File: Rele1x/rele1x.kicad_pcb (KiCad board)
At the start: 2 copper layers, 8 parts, among them J1 TB_1X3, K1 RELAY_C, Q1 2N3904

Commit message: Avances Poncho Rele1x.
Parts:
- added MP?: Plantilla_EDU-CIAA, footprint:Plantilla_EDU-CIAA, F.Cu at (200.0, 92.0)
- moved R1 50.9 mm to (155.0, 96.0), turned to 180 degrees
- moved D1 50.5 mm to (155.0, 104.0), turned to 180 degrees
- moved Q1 48.9 mm to (159.0, 95.0), turned to 270 degrees
- moved R2 41.4 mm to (155.0, 100.0), turned to 180 degrees
- moved LED1 30.4 mm to (159.0, 101.0), turned to 270 degrees
- moved J1 17.5 mm to (150.0, 132.0)
- moved K1 17.5 mm to (150.0, 107.0)
- moved XA1 11.2 mm to (129.0, 92.0)
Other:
- board outline added: 44 x 57 mm

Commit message: Mejoras al ejercicio Rele1x.
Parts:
- removed MP?: Plantilla_EDU-CIAA, footprint:Plantilla_EDU-CIAA
- added G***: LOGO, footprint:Logo_Poncho, F.Cu at (161.0, 127.0)
- added G101: Logo_OSHWA, footprint:Logo_OSHWA, F.Cu at (140.5, 92.0)
- moved Q1 0.50 mm to (159.0, 94.5)
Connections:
- K1 pad 1: Net-(J1-Pad1) -> Net-(J1-Pad2)
- K1 pad 3: Net-(J1-Pad2) -> Net-(J1-Pad1)
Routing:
- net +5VP: track 0.00 -> 54.0 mm
- net Net-(R1-Pad2): track 0.00 -> 43.8 mm
- net Net-(J1-Pad2): track 0.00 -> 25.0 mm
- net Net-(D1-Pad2): track 0.00 -> 24.8 mm
- net Net-(J1-Pad1): track 0.00 -> 11.3 mm
- net Net-(J1-Pad3): track 0.00 -> 11.2 mm
- net Net-(LED1-Pad1): track 0.00 -> 4.41 mm
- net Net-(Q1-Pad2): track 0.00 -> 4.10 mm
- added copper zone on B.Cu, net GNDD
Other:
- net class Default: clearance 0.2 -> 0.5
- rule trace_clearance: 0.2 -> 0.5
- board text added: "Capas: 1 Grilla Posicionamiento: 1 mm Grilla Ruteo: 0,5 mm y 0,25 mm Min ancho pista: 0,8 mm Min ancho pista Q1: 0,6 mm Margen: 0,8 mm Diam Vía/agujero: 1,3/0,7 mm"
- board text added: "NA C NC"
- board text added: "PONCHO RELE1x"

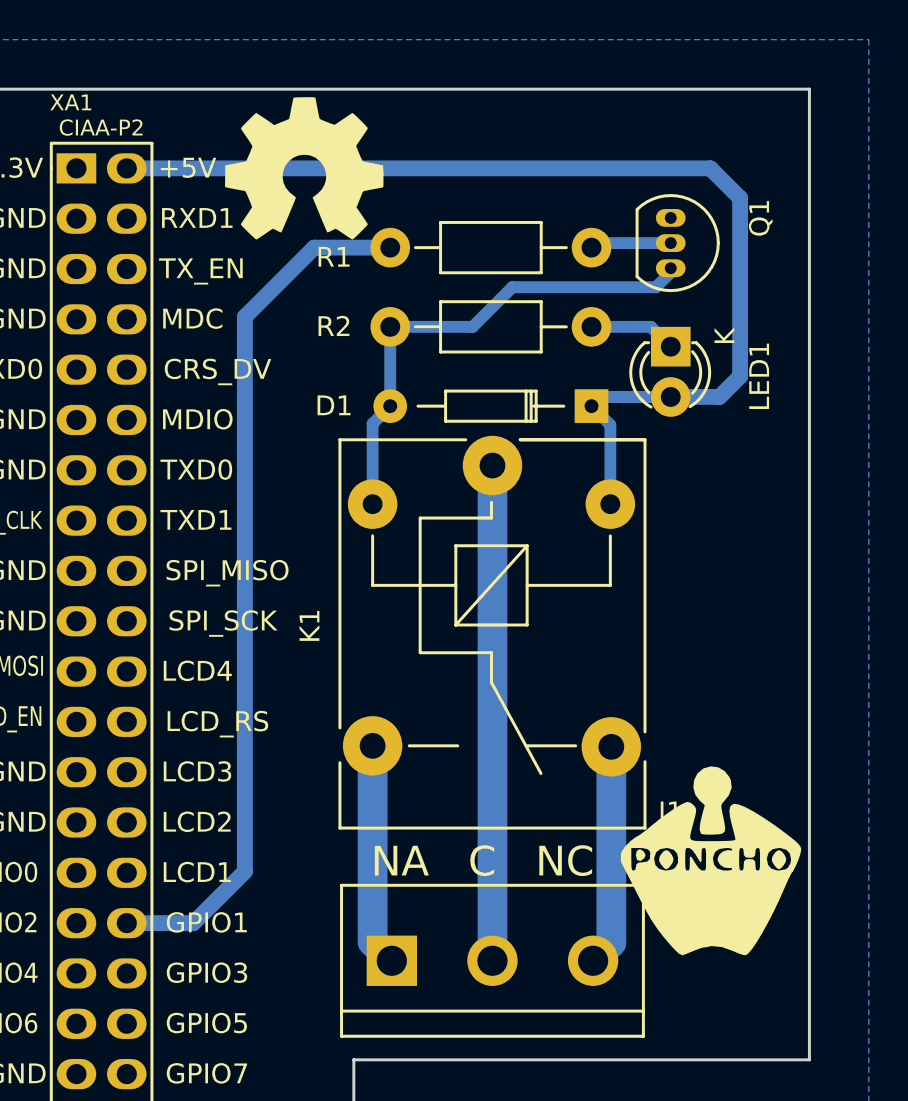
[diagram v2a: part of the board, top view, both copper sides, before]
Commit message: Detalles en el PCB serigrafía, etc.
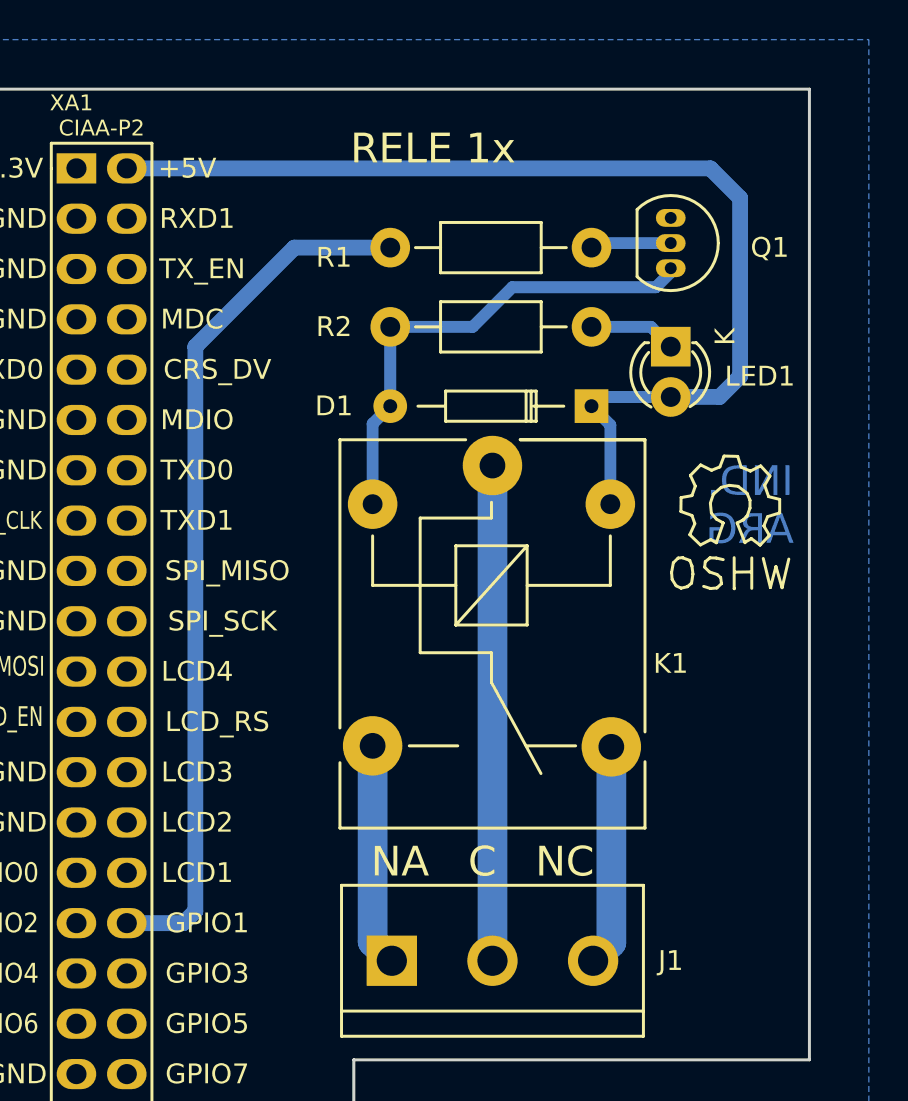
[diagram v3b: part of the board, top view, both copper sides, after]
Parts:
- removed G***: LOGO, footprint:Logo_Poncho
- removed G101: Logo_OSHWA, footprint:Logo_OSHWA
- added REF**: Symbol_OSHW-Logo_SilkScreen, Symbols:Symbol_OSHW-Logo_SilkScreen, F.Cu at (162.0, 109.0)
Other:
- board text added: "Capas: 1 Grilla Posicionamiento: 1 mm Grilla Ruteo: 0,5 mm y 0,25 mm Min ancho pista: 0,8 mm Min ancho pista Q1: 0,6 mm Margen: 0,5 mm Diam Vía/agujero: 1,3/0,7 mm"
- board text added: "IND. ARG"
- board text added: "RELE 1x"
- board text removed: "Capas: 1 Grilla Posicionamiento: 1 mm Grilla Ruteo: 0,5 mm y 0,25 mm Min ancho pista: 0,8 mm Min ancho pista Q1: 0,6 mm Margen: 0,8 mm Diam Vía/agujero: 1,3/0,7 mm"

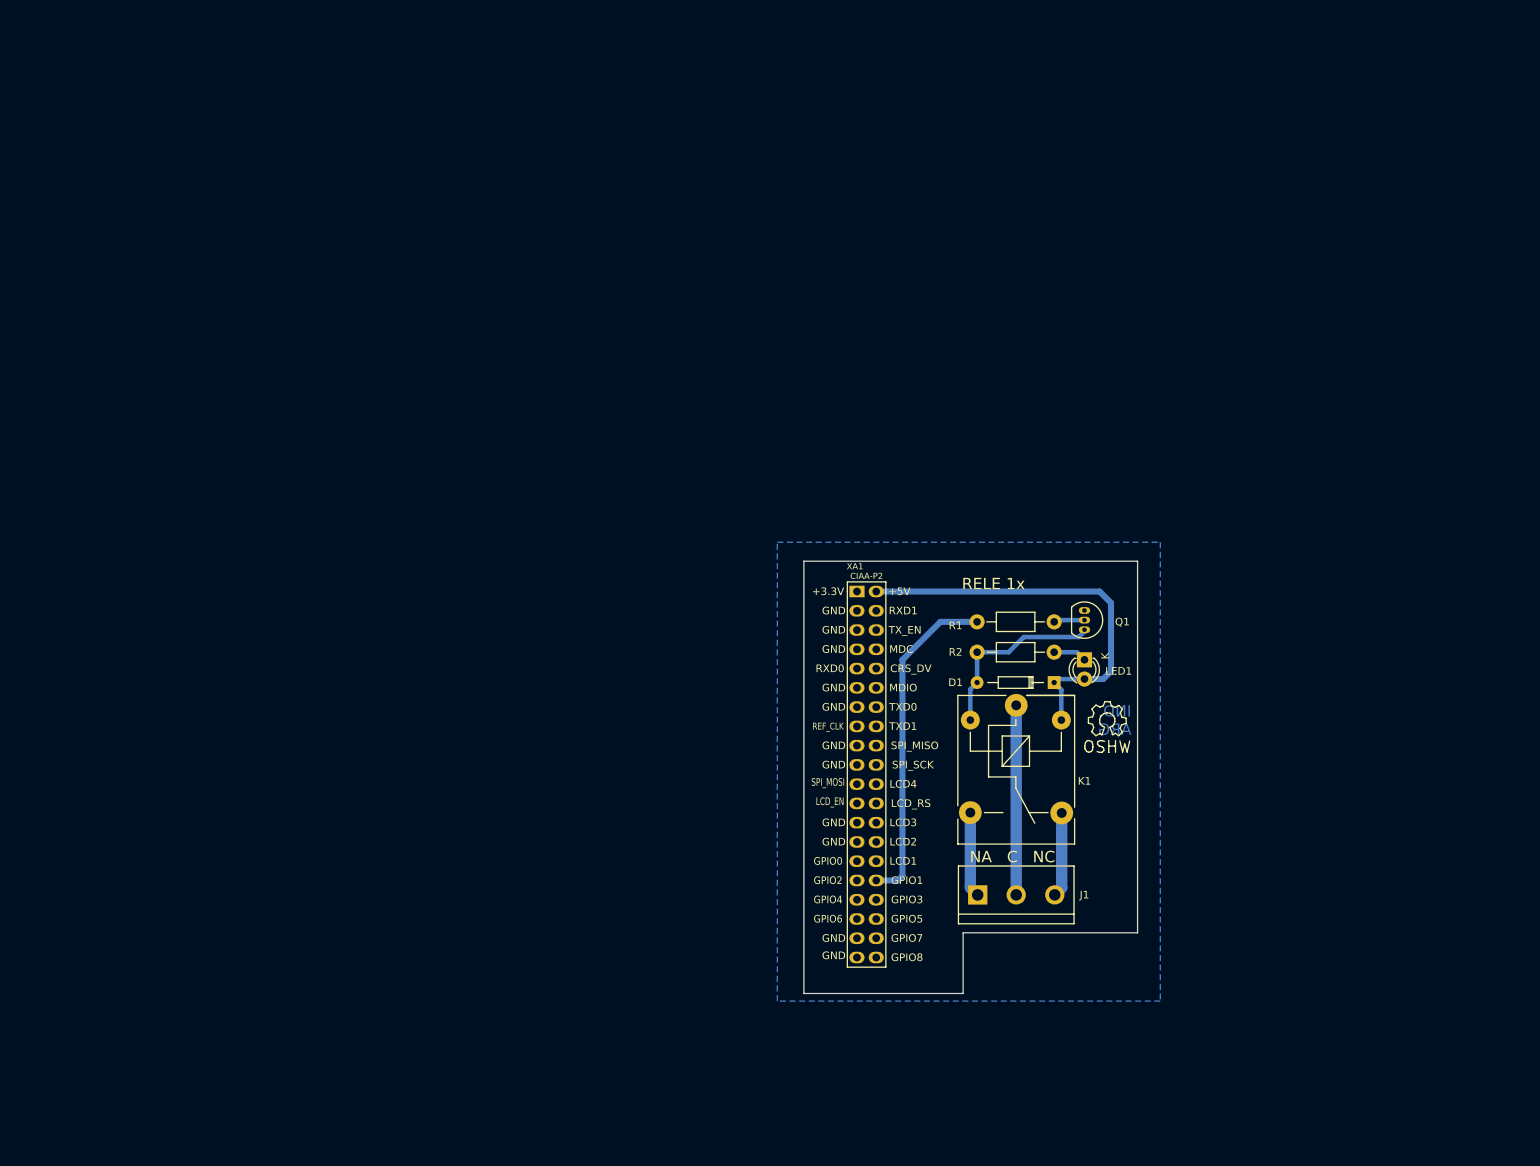
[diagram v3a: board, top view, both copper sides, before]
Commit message: Rele1x: Agrego texto CAPSE, emprolijo pistas, agrego cota, info para array de impresión. Agrego impresiones.
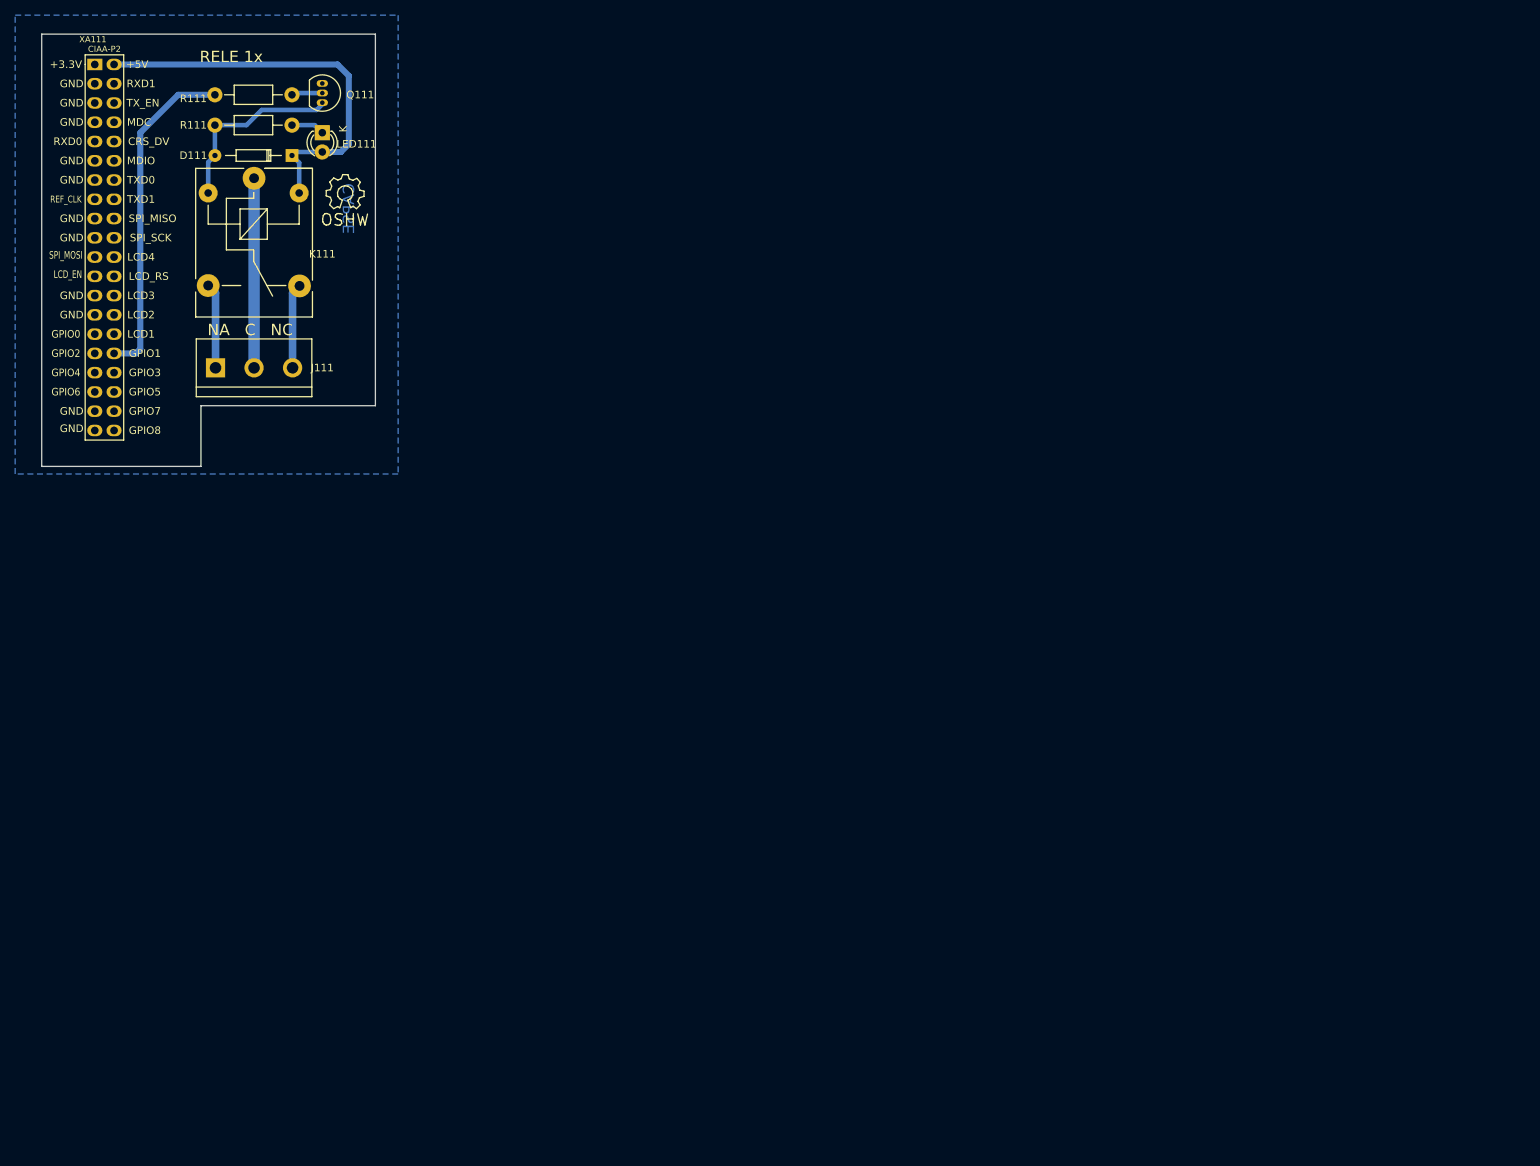
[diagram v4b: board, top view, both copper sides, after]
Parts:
- moved D111 122.2 mm to (54.5, 34.5)
- moved J111 122.2 mm to (49.5, 62.5)
- moved K111 122.2 mm to (49.5, 37.5)
- moved LED111 122.2 mm to (58.5, 31.5)
- moved Q111 122.2 mm to (58.5, 25.0)
- moved R111 122.2 mm to (54.5, 26.5)
- moved R111 122.2 mm to (54.5, 30.5)
- moved REF**111 122.2 mm to (61.5, 39.5)
- moved XA111 122.2 mm to (28.5, 22.5)
- renumbered D1 to D111, J1 to J111, K1 to K111, LED1 to LED111, Q1 to Q111, R1 to R111, R2 to R111, REF** to REF**111, XA1 to XA111
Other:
- board text added: "CAPSE"
- board text added: "Capas: 1 Grilla Posicionamiento: 1 mm Grilla Ruteo: 0,5 mm y 0,25 mm Min ancho pista: 0,8 mm Min ancho pista Q1: 0,6 mm Margen: 0,5 mm Diam Vía/agujero: 1,3/0,7 mm Array: 2x3 75x90 mm"
- board text removed: "Capas: 1 Grilla Posicionamiento: 1 mm Grilla Ruteo: 0,5 mm y 0,25 mm Min ancho pista: 0,8 mm Min ancho pista Q1: 0,6 mm Margen: 0,5 mm Diam Vía/agujero: 1,3/0,7 mm"
- board text removed: "IND. ARG"
